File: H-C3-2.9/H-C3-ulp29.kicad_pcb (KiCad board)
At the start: 4 copper layers, 83.4 x 42.1 mm, 54 parts, among them CN1 HX JN1.27-2X5 TP H4.9, J1 USB_C_Receptacle_USB2.0, J2 AFC24-S24FIC-00, J4 SM04B-SRSS-TB_LF__SN_, Q1 Si1308, Q2 Si2301CDS, SW1 TM-2023, SW3 K2-1806SQ-A2DW-04, U1 E73-2G4M08S1C, U2 MCP1700-3302E_SOT23, U8 PCF8563T, Y1 Crystal_Small, Y2 RTC_Crystal_32MHz

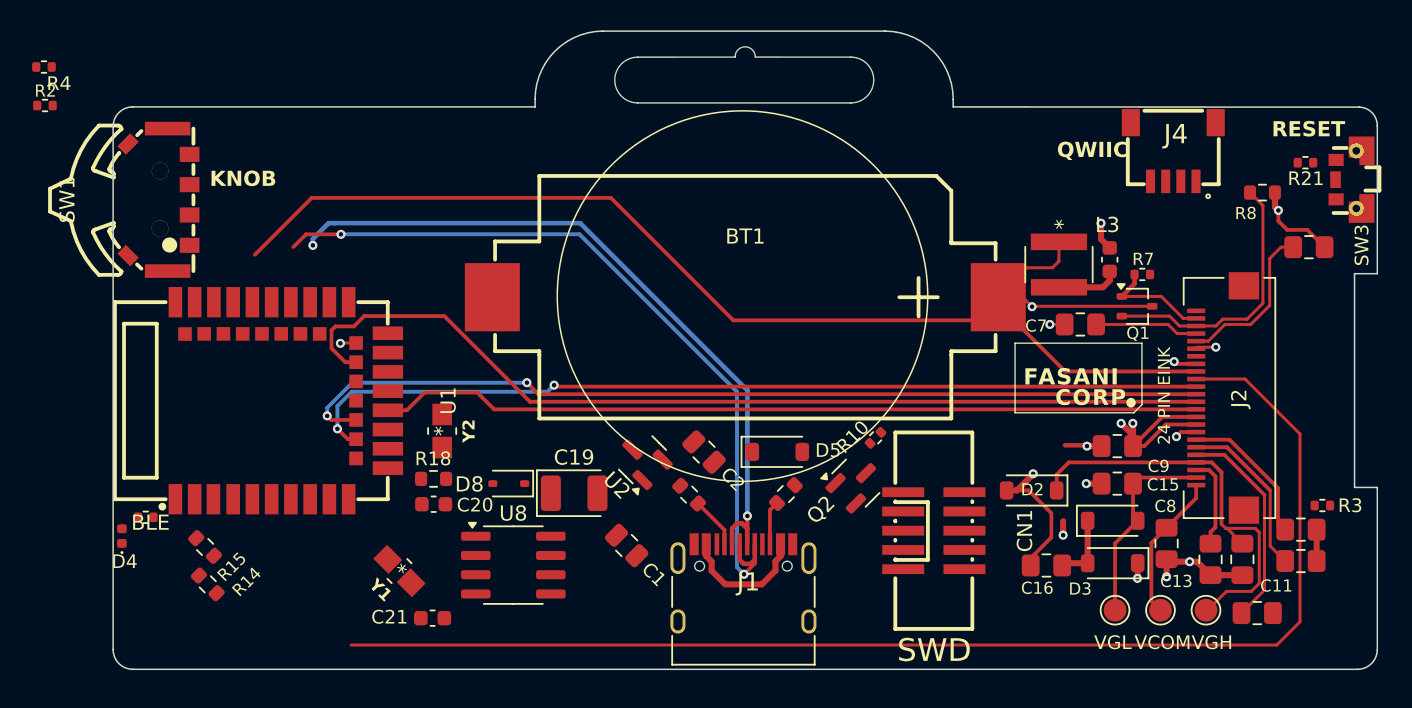
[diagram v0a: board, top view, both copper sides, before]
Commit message: RTC is out, use internal one
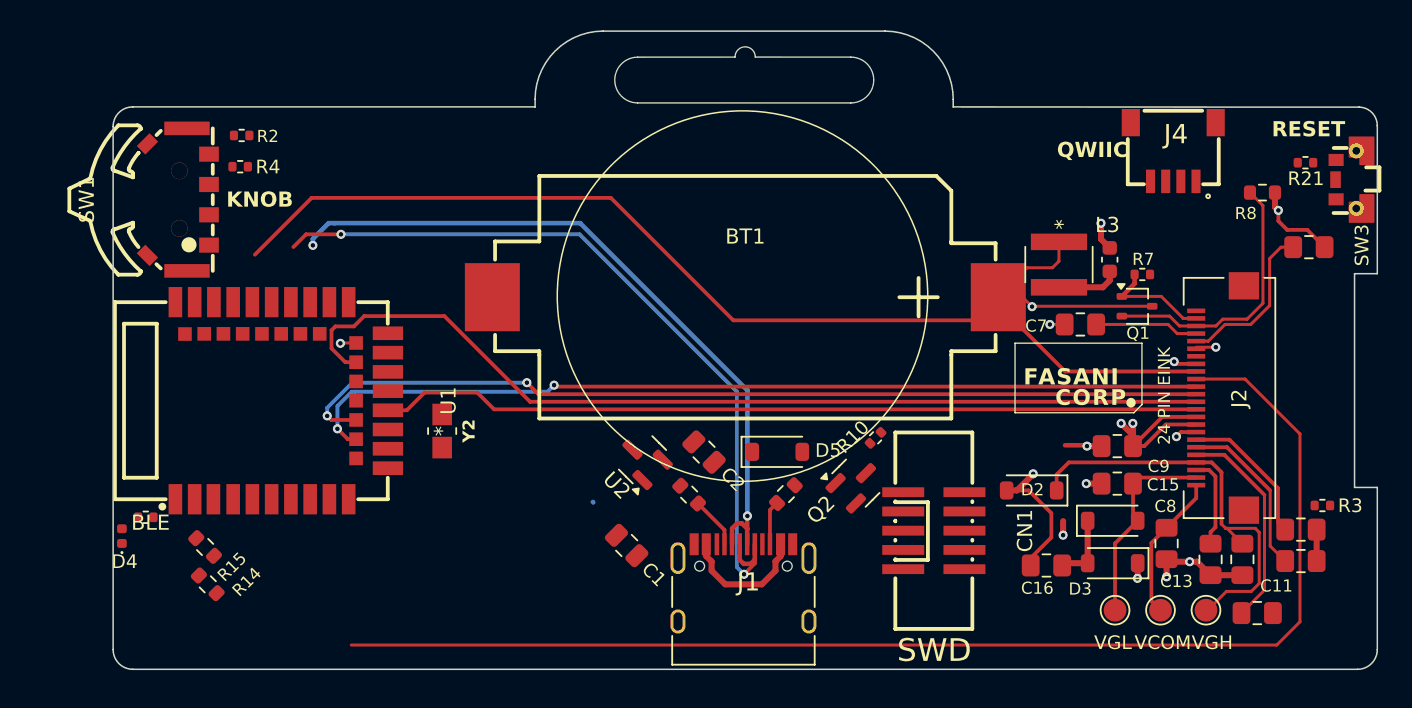
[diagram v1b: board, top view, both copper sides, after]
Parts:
- removed C19: C_Polarized 100uF, Capacitor_Tantalum_SMD:CP_EIA-3528-21_Kemet-B
- removed C20, C21: 12 pF, Capacitor_SMD:C_0603_1608Metric
- removed D8: 1N4148WS, Diode_SMD:D_SOD-323
- removed R18: 10 K, Resistor_SMD:R_0603_1608Metric
- removed U8: PCF8563T, Package_SO:SOIC-8_3.9x4.9mm_P1.27mm
- removed Y1: Crystal_Small, footprints:Q13FC1350000400-Crystal
- moved R4 14.5 mm to (94.5, 48.4)
- moved R2 13.1 mm to (94.6, 46.4)
- moved SW1 1.28 mm to (90.4, 50.6)

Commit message: Pre-release please check routing
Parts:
- added R6: 470k, Resistor_SMD:R_0402_1005Metric, F.Cu at (98.2, 74.9)
- added R9: 470k, Resistor_SMD:R_0402_1005Metric, F.Cu at (99.6, 76.3)
- moved R3 69.7 mm to (96.3, 73.5), turned to 135 degrees
- moved C1 3.96 mm to (118.9, 69.6)
- moved R10 3.40 mm to (133.3, 67.7), turned to -135 degrees
- moved R2 2.95 mm to (94.7, 49.3), turned to 180 degrees
- moved R4 2.55 mm to (94.7, 45.9), turned to 180 degrees
- moved Y2 1.95 mm to (107.1, 67.7)
- moved C10 1.01 mm to (164.4, 73.4)
- moved C12 1.01 mm to (164.4, 75.5)
- moved CN1 0.62 mm to (140.7, 72.9)
- moved L3 0.54 mm to (149.0, 54.9)
- moved C17 0.44 mm to (152.3, 54.5)
- moved D4 0.31 mm to (86.8, 73.1)
- moved R7 0.06 mm to (154.0, 55.5)
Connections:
- net Net-(BT1-+) renamed +VBAT
- CN1 pad 5: SWO ?? -> unconnected-(CN1-Pad5)
- U1 pad 42: unconnected-(U1-P1.06-Pad42) -> SW0
- U1 pad 7: unconnected-(U1-AI0-Pad7) -> Net-(U1-AI0)
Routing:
- net /SDA: track 0.00 -> 123.6 mm, vias 0 -> 2
- net /SCL: track 0.00 -> 121.6 mm
- net /MCU_RST: track 0.00 -> 101.1 mm, vias 0 -> 3
- net SWDIO: track 0.00 -> 64.0 mm, vias 0 -> 2
- net SWCLK: track 0.00 -> 61.4 mm, vias 0 -> 2
- net +VBAT: track 0.00 -> 59.7 mm, vias 0 -> 2
- net +VBUS: track 8.73 -> 57.9 mm, vias 0 -> 2
- net GND: track 27.7 -> 71.3 mm, vias 12 -> 28
- net +VIN: track 0.00 -> 27.4 mm
- net +3V3: track 17.3 -> 37.9 mm, vias 2 -> 13
- net Net-(R4-Pad2): track 0.00 -> 16.7 mm
- net SW2: track 0.00 -> 16.0 mm, vias 0 -> 2
- net SW0: track 0.00 -> 14.5 mm, vias 0 -> 2
- net /EPD_RST: track 84.0 -> 98.2 mm
- net Net-(U1-P1.13): track 0.00 -> 13.1 mm
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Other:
- board text removed: "19"

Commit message: FAB attempt 1
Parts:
- added J3: Conn_01x05, Connector_PinHeader_2.54mm:PinHeader_1x07_P2.54mm_Vertical, F.Cu at (104.8, 78.3)
- moved J4 78.2 mm to (86.4, 73.8), turned to -90 degrees
- moved R15 5.68 mm to (96.5, 77.2)
- moved R14 3.12 mm to (94.9, 77.7)
- moved D4 1.24 mm to (86.8, 71.9)
- moved R5 0.32 mm to (88.5, 71.8)
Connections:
- U1 pad 12: unconnected-(U1-P0.26-Pad12) -> /P0.26
- U1 pad 32: unconnected-(U1-P0.20-Pad32) -> /P0.20
- U1 pad 33: unconnected-(U1-P0.13-Pad33) -> /P0.13
- U1 pad 34: unconnected-(U1-P0.22-Pad34) -> /P0.22
- U1 pad 36: unconnected-(U1-P1.00-Pad36) -> /P1.00
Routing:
- net /SDA: track 123.6 -> 12.4 mm, vias 2 -> 0
- net /SCL: track 121.6 -> 13.7 mm
- net /P0.13: track 0.00 -> 41.2 mm, vias 0 -> 1
- net /P0.20: track 0.00 -> 24.4 mm, vias 0 -> 1
- net /P0.22: track 0.00 -> 23.5 mm, vias 0 -> 1
- net /P1.00: track 0.00 -> 23.0 mm, vias 0 -> 1
- net /P0.26: track 0.00 -> 17.3 mm
- net +3V3: track 37.9 -> 42.6 mm
- net +VBAT: track 59.7 -> 63.6 mm
- net /EPD_RST: track 98.2 -> 100.8 mm
- net SW2: track 16.0 -> 18.1 mm
- net GND: track 71.3 -> 69.2 mm, vias 28 -> 29
- net /MCU_RST: track 101.1 -> 99.2 mm
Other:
- board text added: "3V3"
- board text added: "BitBadger"
- board text added: "GND"
- board text added: "P0.13"
- board text added: "P0.20"
- board text added: "P0.22"
- board text added: "P0.26"
- board text added: "P1.00"
- board text added: "nRF52840"
- board text removed: "BLE"
- board text removed: "KNOB"

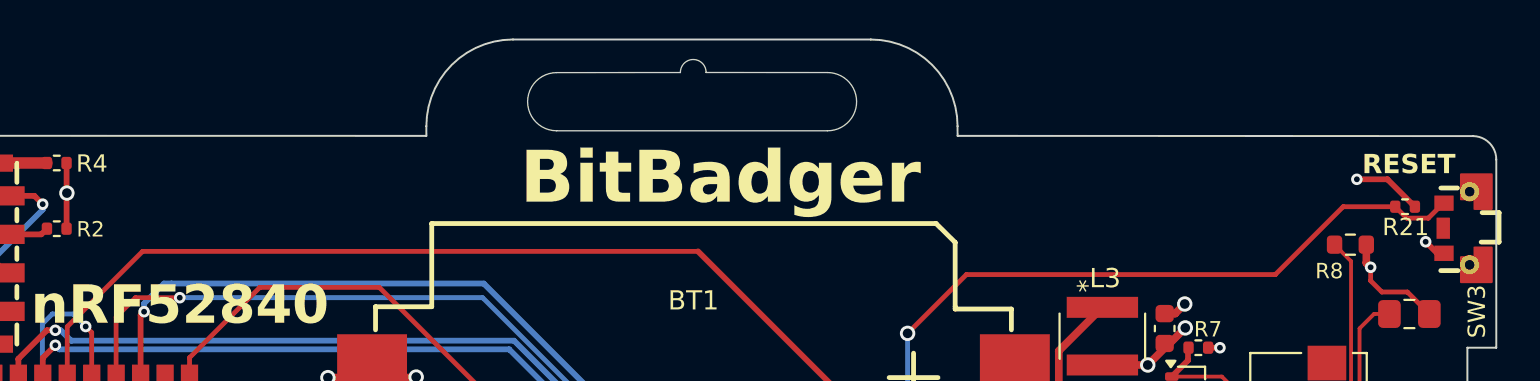
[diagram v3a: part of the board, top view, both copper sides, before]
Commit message: Modified front silkscreen info
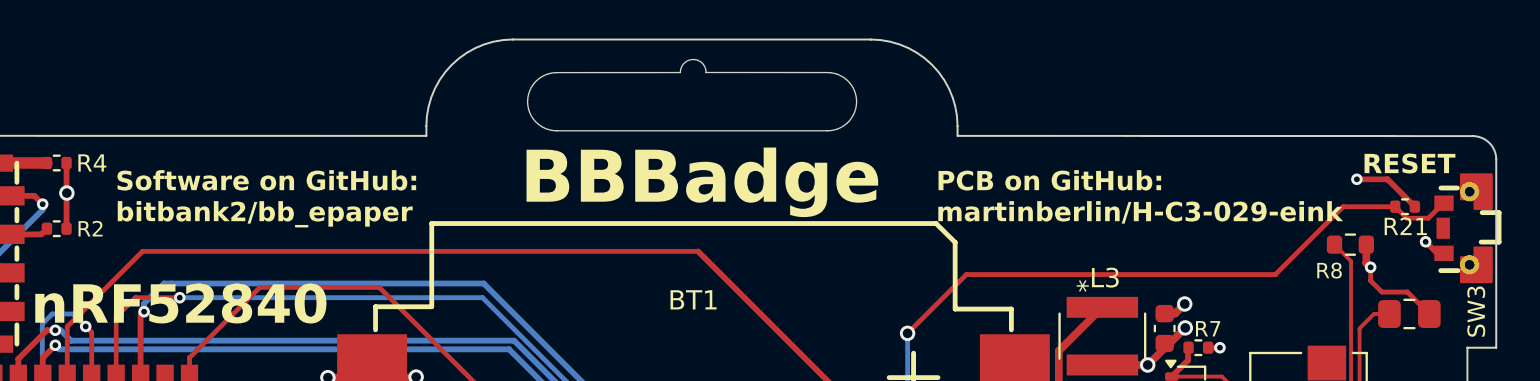
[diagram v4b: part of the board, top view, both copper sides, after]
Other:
- board text added: "BBBadge"
- board text added: "PCB on GitHub: martinberlin/H-C3-029-eink"
- board text added: "Software on GitHub: bitbank2/bb_epaper"
- board text removed: "BitBadger"

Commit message: Updated for 1.1
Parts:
- added C18: C_Pol 100uF, footprints:C7171_CAP, F.Cu at (110.4, 61.9)
- added C3: 15pF, Capacitor_SMD:C_0402_1005Metric, F.Cu at (109.1, 70.2)
- added C4: 15pF, Capacitor_SMD:C_0402_1005Metric, F.Cu at (109.1, 65.2)
- added C5: 100nF, Capacitor_SMD:C_0402_1005Metric, F.Cu at (108.5, 63.5)
- J3: value Conn_01x05 -> Conn_01x07
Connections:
- SW1 pad C: SW0 -> Net-(R2-Pad2)
- SW1 pad T: Net-(R2-Pad2) -> SW0
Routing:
- net GND: track 69.2 -> 76.0 mm, vias 29 -> 32
- net SWDIO: track 63.9 -> 70.6 mm
- net +3V3: track 42.6 -> 45.4 mm
- net Net-(U1-XL2): track 3.07 -> 5.18 mm
- net Net-(U1-XL1): track 3.09 -> 5.18 mm
- net /MCU_RST: track 99.2 -> 101.0 mm
- net Net-(R2-Pad2): track 1.93 -> 3.43 mm
- net unconnected-(J2-Pad19): track 1.30 -> 0.00 mm, vias 1 -> 0
- net /EPD_CLK: track 60.3 -> 61.5 mm
- net /EPD_MOSI: track 54.3 -> 53.3 mm
- net SW0: track 14.5 -> 15.2 mm
- net /EPD_DC: track 59.4 -> 59.9 mm
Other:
- outline, holes or cut-outs redrawn
